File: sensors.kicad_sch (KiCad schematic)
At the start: 3 parts

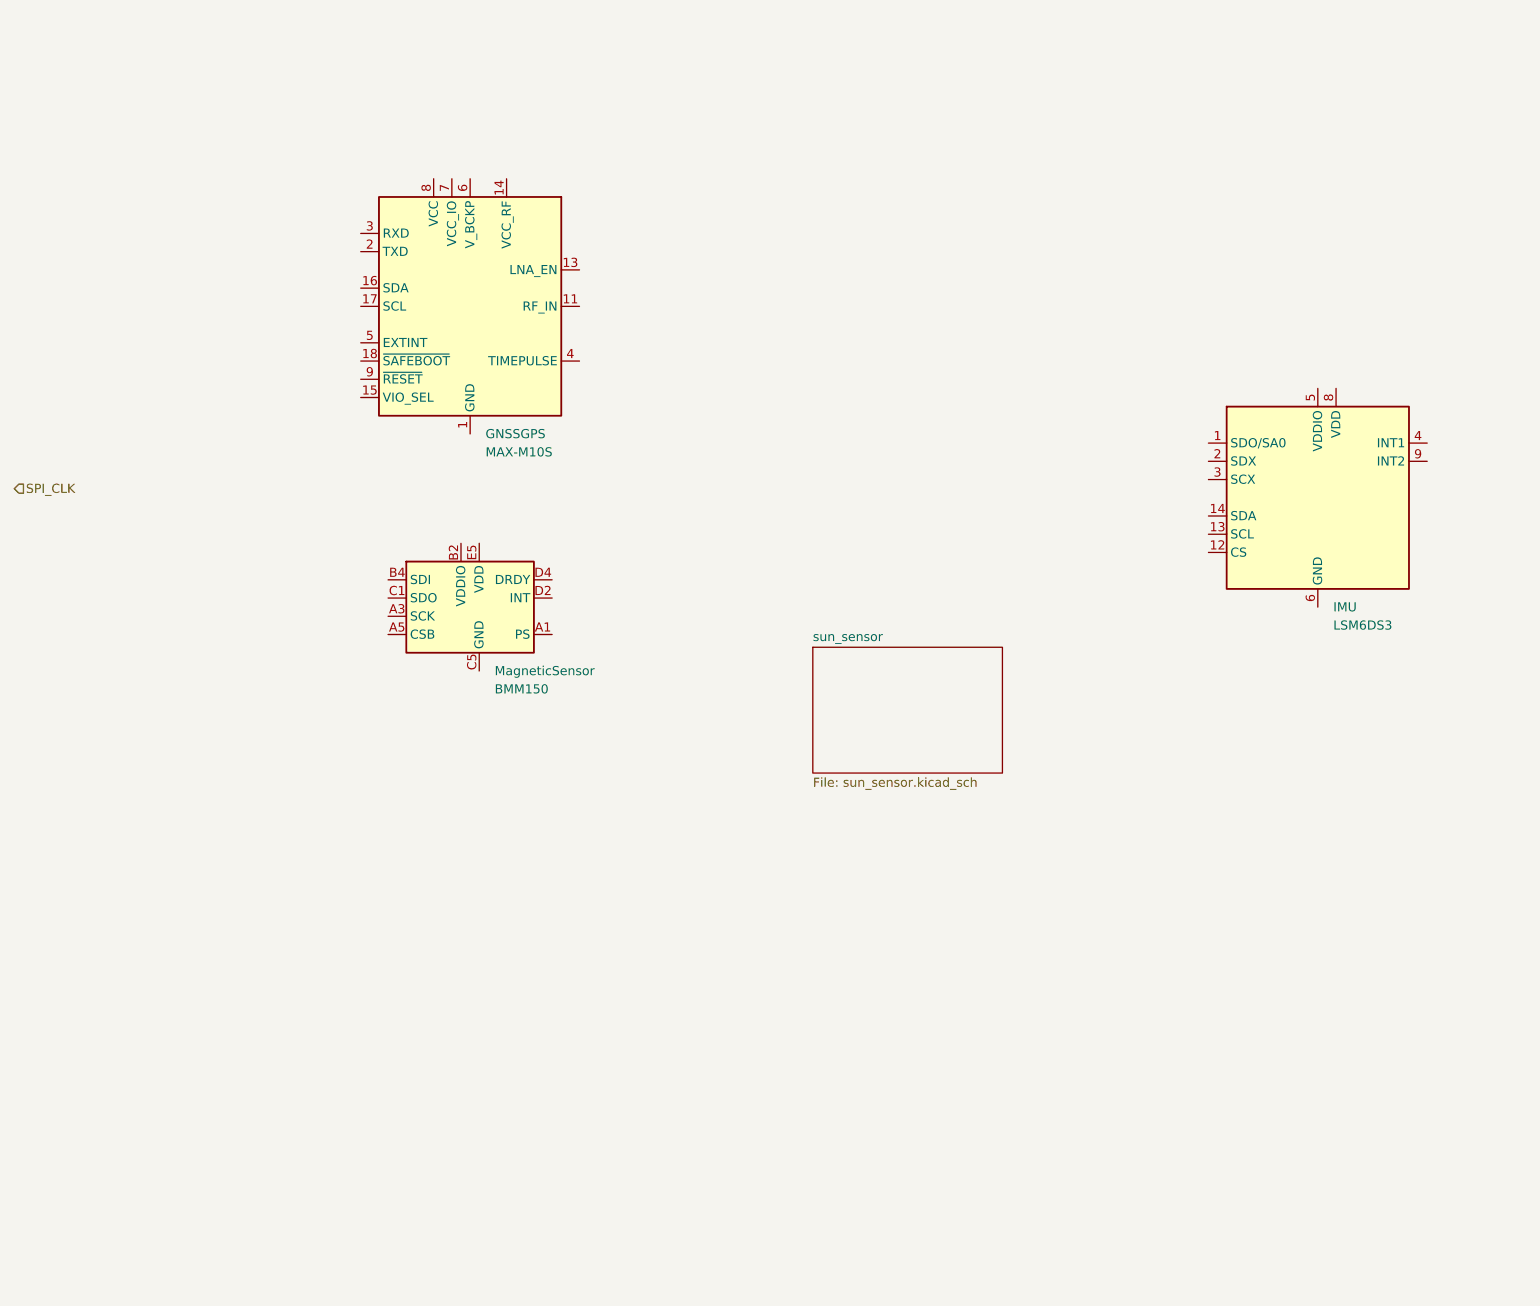
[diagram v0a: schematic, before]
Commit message: Updated sensors wiring (connected pins to +3V3 and GND), added pullups and decouplers. Double check my wiring as these could be wrong.
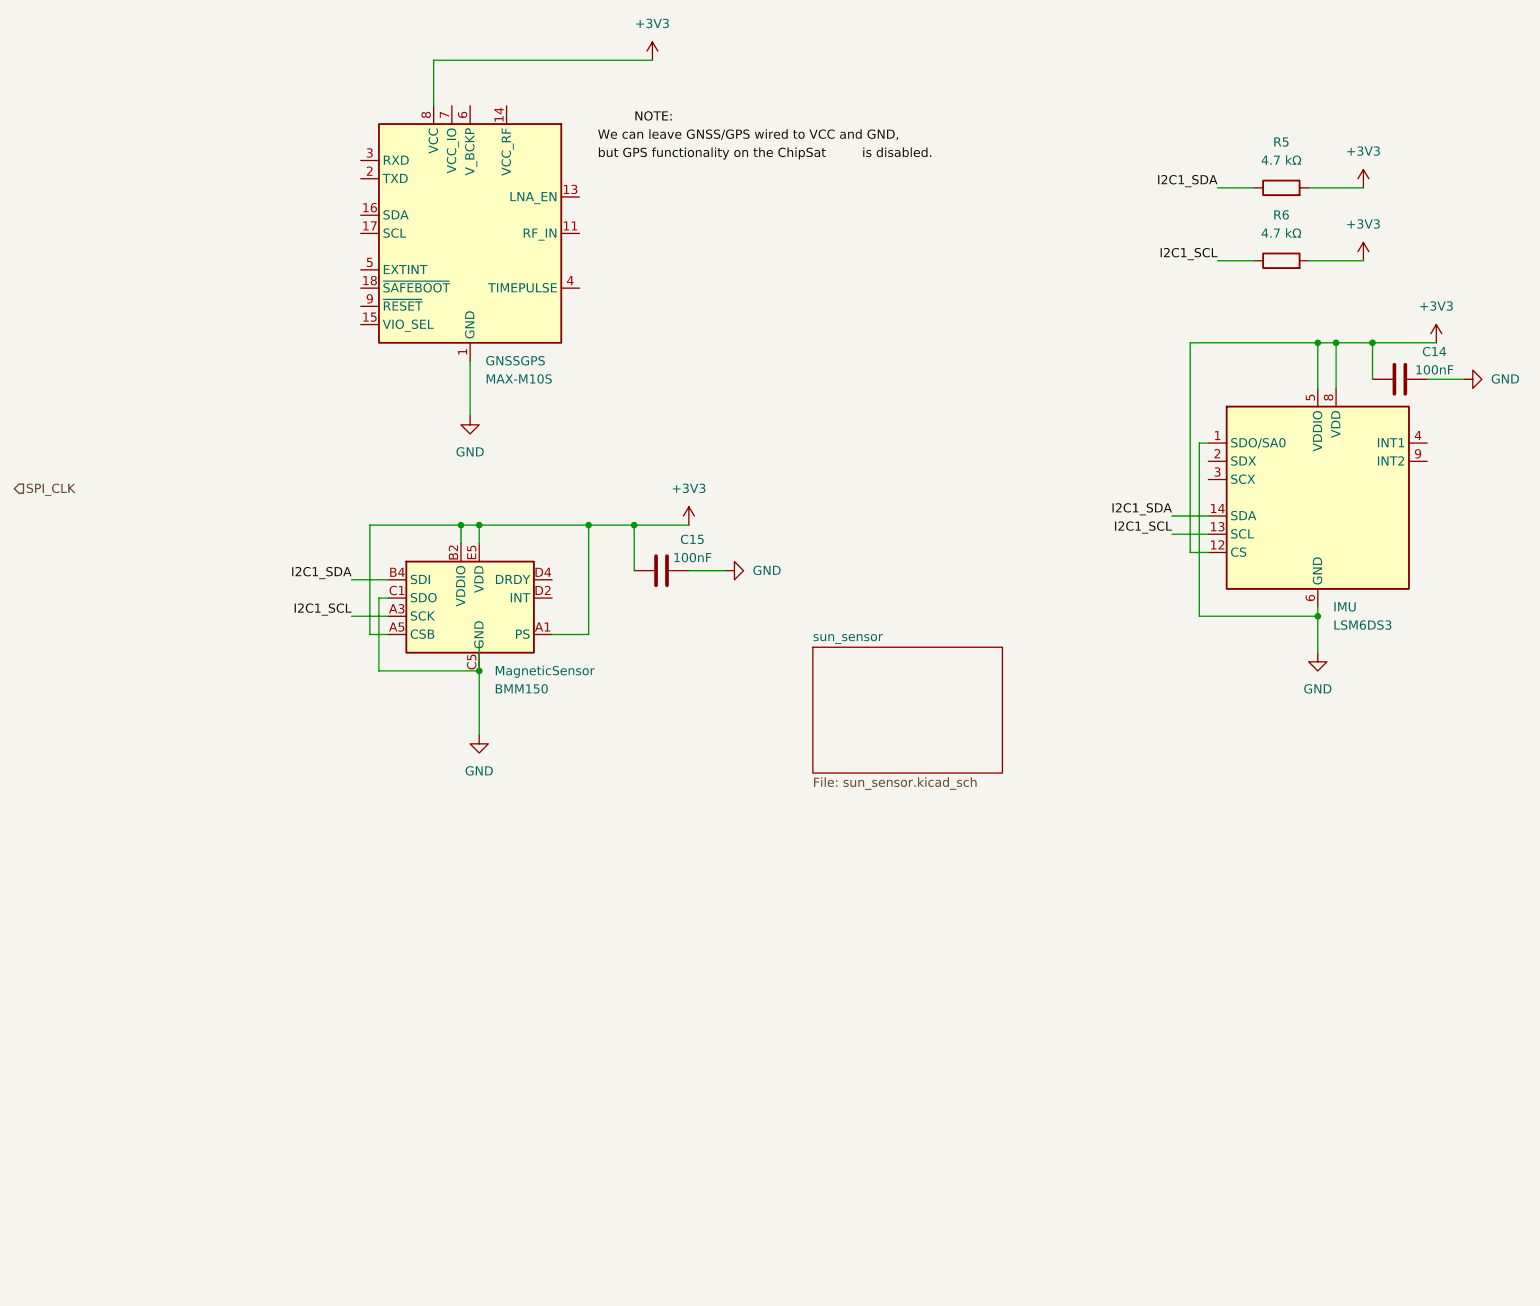
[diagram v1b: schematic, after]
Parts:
- added C14, C15: 100nF, symbol Device:C
- added R5, R6: 4.7 kΩ, symbol Device:R
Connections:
- net +3V3: now reaches MagneticSensor.A1 (PS)
- net +3V3: now also GNSSGPS.8 (VCC), IMU.12 (CS), IMU.5 (VDDIO), IMU.8 (VDD), MagneticSensor.A5 (CSB), MagneticSensor.B2 (VDDIO), MagneticSensor.E5 (VDD), C14.1, C15.1, R5.2, R6.2
- net I2C1_SCL: now reaches MagneticSensor.A3 (SCK)
- net I2C1_SCL: now also IMU.13 (SCL), R6.1
- net I2C1_SDA: now reaches MagneticSensor.B4 (SDI)
- net I2C1_SDA: now also IMU.14 (SDA), R5.1
- net GND: now reaches MagneticSensor.C1 (SDO)
- net GND: now also GNSSGPS.1 (GND), GNSSGPS.10 (GND), GNSSGPS.12 (GND), IMU.1 (SDO/SA0), IMU.6 (GND), IMU.7 (GND), MagneticSensor.C5 (GND), MagneticSensor.E1 (GND), MagneticSensor.E3 (GND), C14.2, C15.2
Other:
- moved on the sheet: GNSSGPS

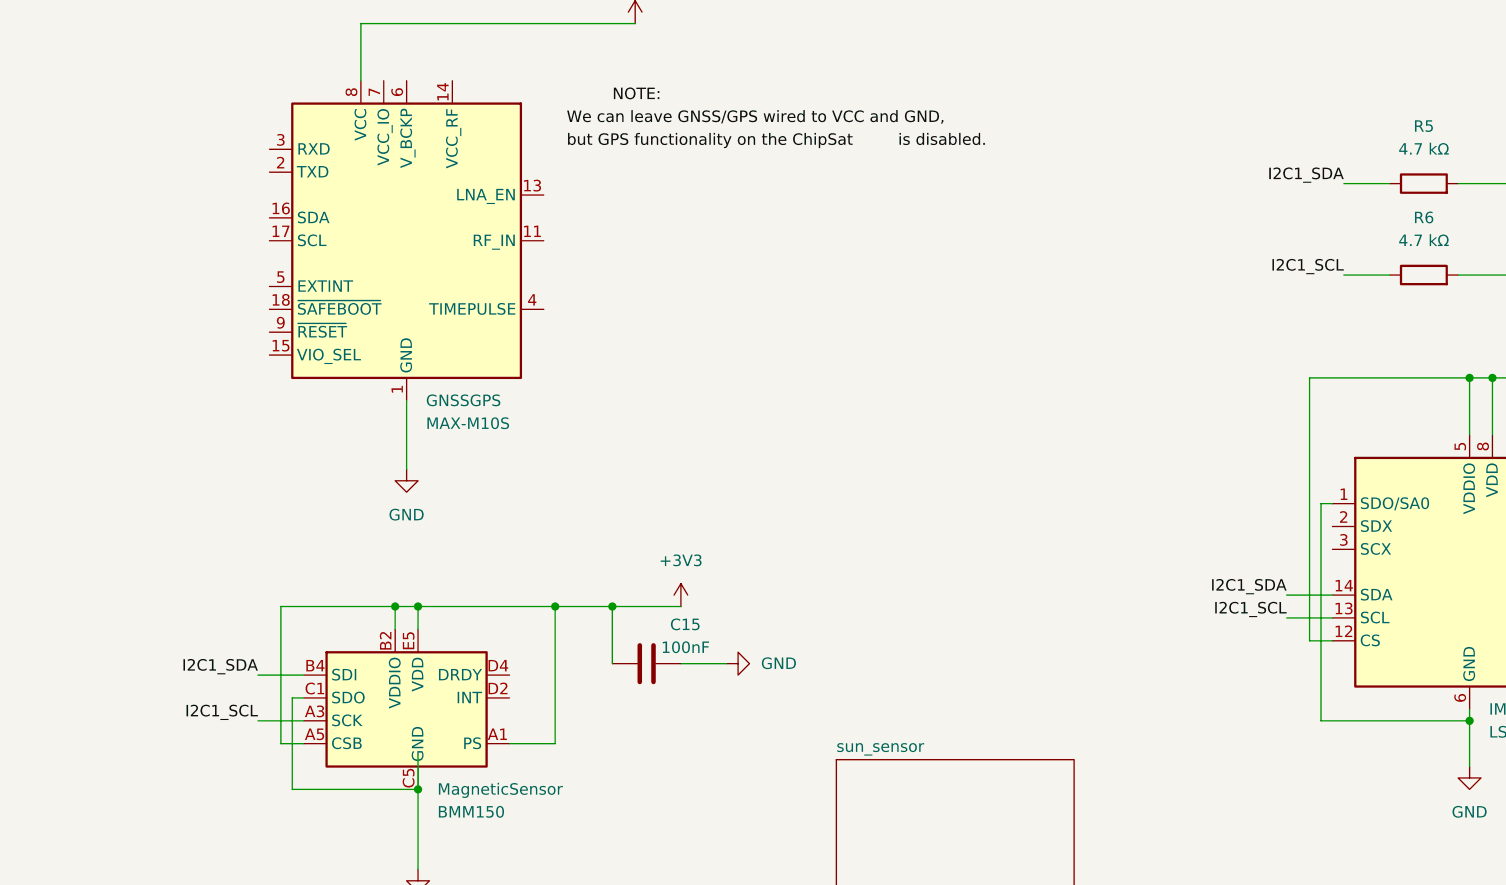
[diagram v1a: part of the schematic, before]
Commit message: Complete STM32 subsystem integration and schematic review
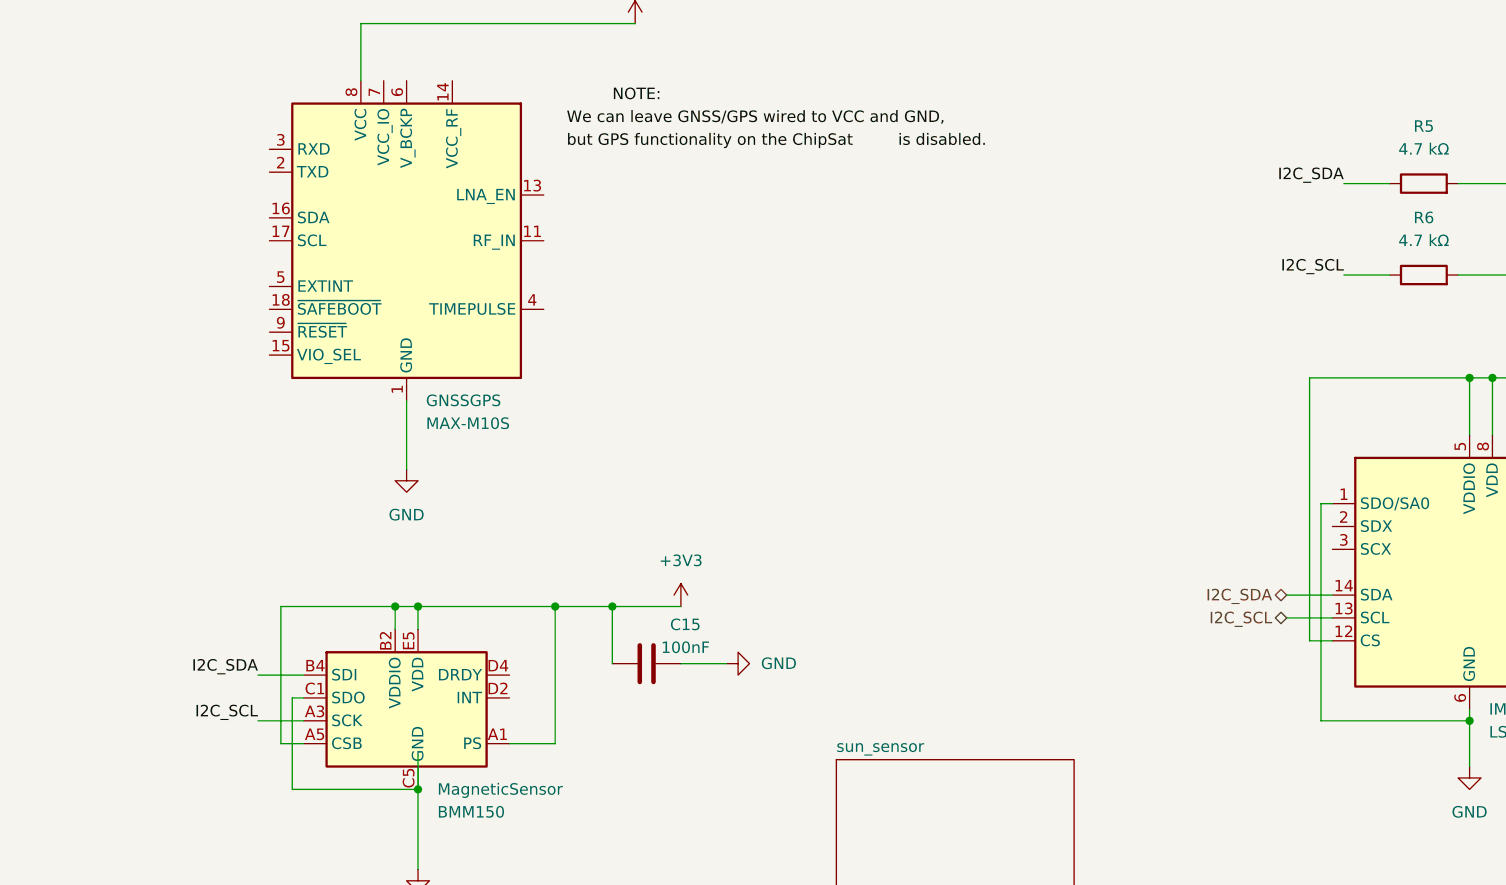
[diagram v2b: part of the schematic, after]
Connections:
- net I2C1_SCL renamed I2C_SCL
- net I2C1_SDA renamed I2C_SDA
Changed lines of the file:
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@@
 		)
 	)
-	(label "I2C1_SDA"
+	(label "I2C_SDA"
 		(at 207.01 43.18 180)
-		(effects
-			(font
-				(size 1.27 1.27)
-			)
-			(justify right bottom)
-		)
-	)
-	(label "I2C1_SDA"
-		(at 200.66 88.9 180)
 		(effects
 			(font
@@
 		)
 	)
-	(label "I2C1_SCL"
+	(label "I2C_SCL"
 		(at 86.36 102.87 180)
 		(effects
@@
 		)
 	)
-	(label "I2C1_SCL"
+	(label "I2C_SCL"
 		(at 207.01 53.34 180)
-		(effects
-			(font
-				(size 1.27 1.27)
-			)
-			(justify right bottom)
-		)
-	)
-	(label "I2C1_SCL"
-		(at 200.66 91.44 180)
 		(effects
 			(font
@@
 		)
 	)
-	(label "I2C1_SDA"
+	(label "I2C_SDA"
 		(at 86.36 97.79 180)
 		(effects
@@
 		)
 	)
+	(hierarchical_label "I2C_SCL"
+		(shape bidirectional)
+		(at 200.66 91.44 180)
+		(effects
+			(font
+				(size 1.27 1.27)
+			)
+			(justify right)
+		)
+	)
 	(hierarchical_label "SPI_CLK"
 		(shape input)
@@
 		)
 	)
+	(hierarchical_label "I2C_SDA"
+		(shape bidirectional)
+		(at 200.66 88.9 180)
+		(effects
+			(font
+				(size 1.27 1.27)
+			)
+			(justify right)
+		)
+	)
